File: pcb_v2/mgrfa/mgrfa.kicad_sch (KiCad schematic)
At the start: 20 parts, among them J1 sr8a_A, J10 designador, J2 sr8a_B, J3 sr8a_C, J4 sr8a_D, J5 sr8a_E, J6 sr8a_H, J7 sr8a_L, J8 bus_mgrf_1, J9 bus_mgrf_2, U1 74LS244, U2 74LS244

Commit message: arquivos no note
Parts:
- C1, C2: footprint (none) -> Capacitor_THT:C_Disc_D5.1mm_W3.2mm_P5.00mm

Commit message: projeto enviado para impressao em dezembro/25
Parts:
- D1: value LED -> POWER
- D2: value LED -> READ
- D3: value LED -> WRITE
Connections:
- net +5V: now also J8.1 (Pin_1); no longer J8.4 (Pin_4), J8.6 (Pin_6), J8.8 (Pin_8)
- net GND: now also J8.15 (Pin_15); no longer J8.10 (Pin_10), J8.12 (Pin_12), J8.14 (Pin_14)
- net data_0: now also J8.14 (Pin_14); no longer J8.15 (Pin_15)
- net data_7: now also J8.4 (Pin_4); no longer J8.1 (Pin_1)
- no-connect marks 46 -> 50

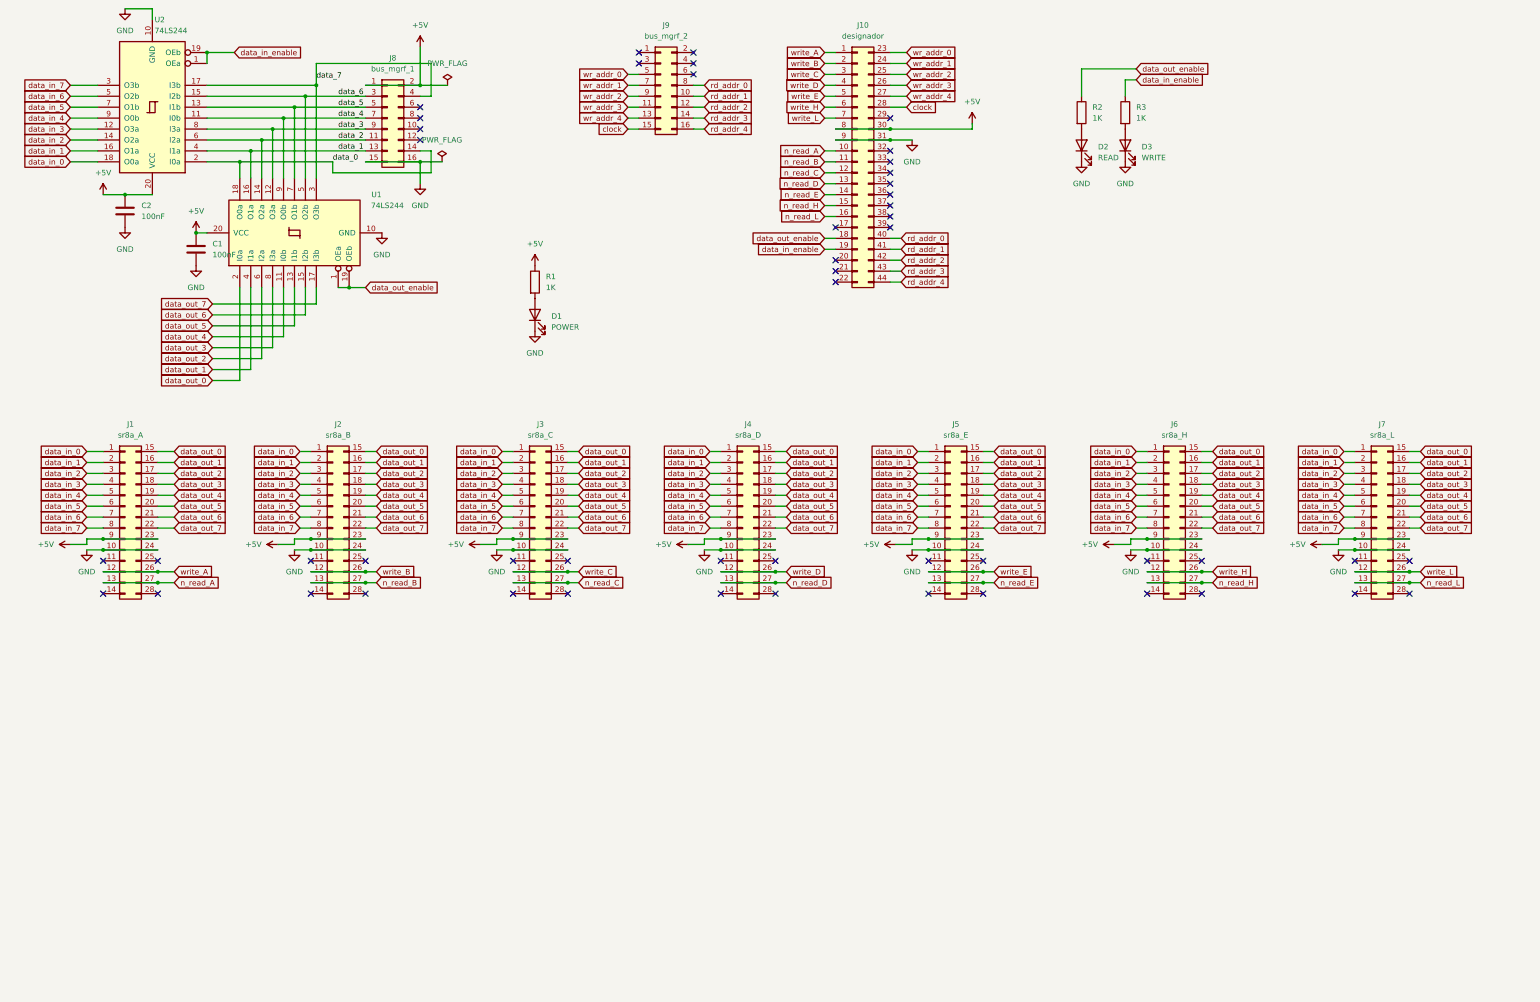
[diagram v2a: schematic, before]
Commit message: inicio da revisao completa; a placa sr8 será removida e incorporada aqui
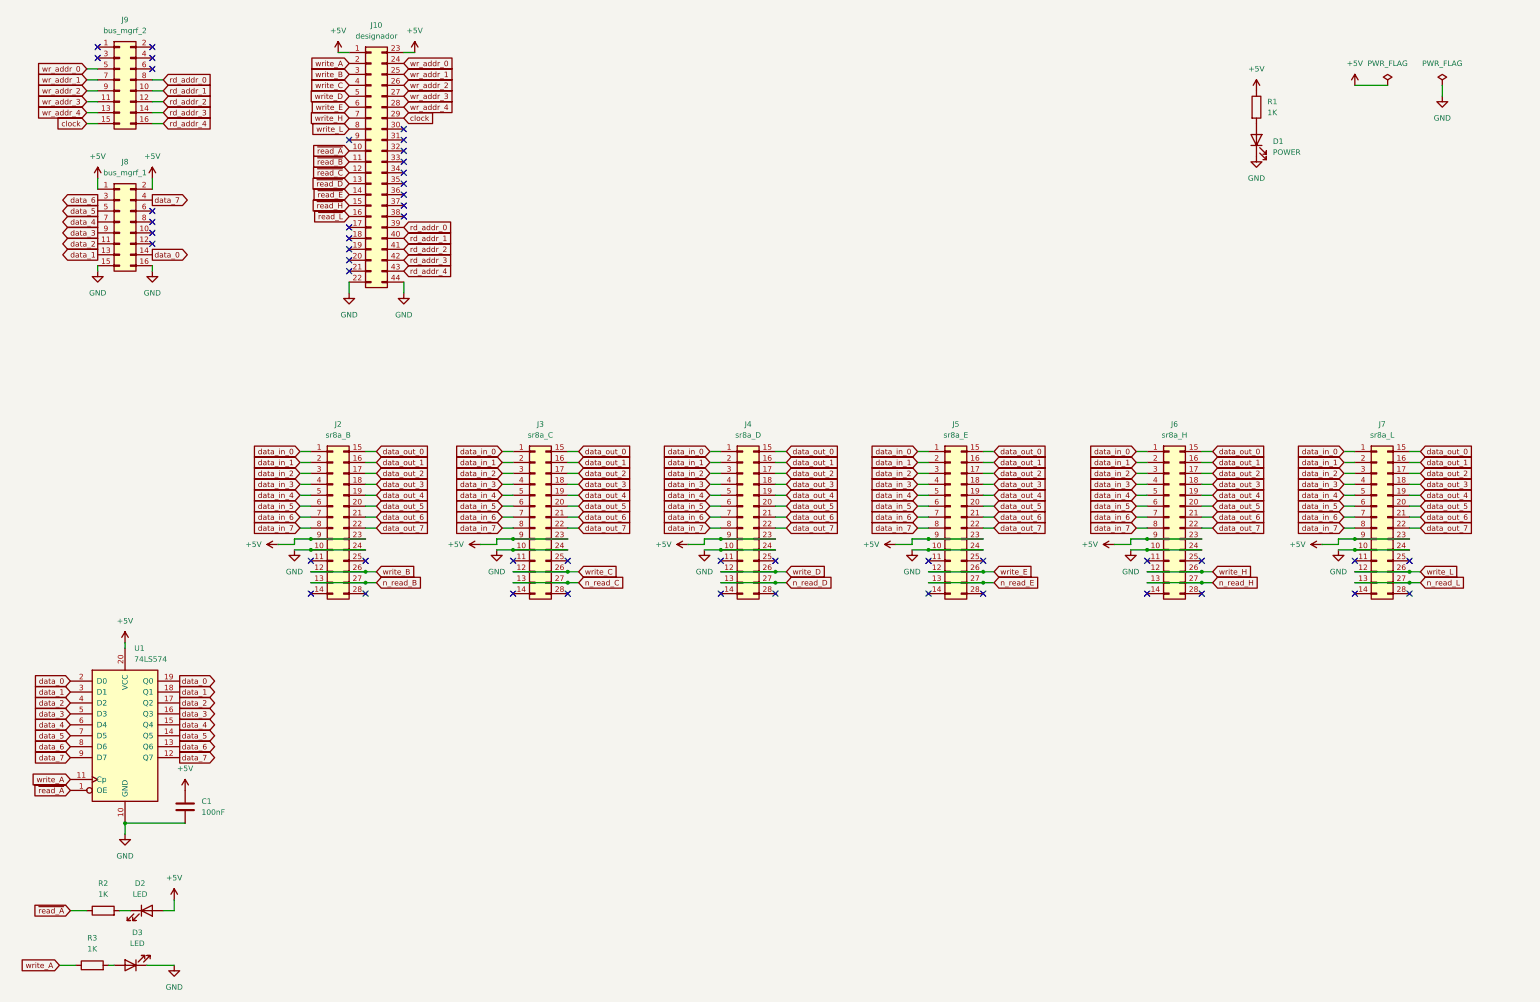
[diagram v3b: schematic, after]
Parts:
- removed C2: 100nF, Capacitor_THT:C_Disc_D5.1mm_W3.2mm_P5.00mm, symbol Device:C
- removed J1: sr8a_A, edge_connector:male-edge-connector-28, symbol Connector_Generic:Conn_02x14_Top_Bottom
- removed U1, U2: 74LS244, Package_DIP:DIP-20_W7.62mm, symbol 74xx:74LS244
- added U1: 74LS574, Package_DIP:DIP-20_W7.62mm, symbol 74xx:74LS574
- D2: value READ -> LED
- D3: value WRITE -> LED
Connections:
- net +5V: now also D2.2 (A), J10.1 (Pin_1), J10.23 (Pin_23), U1.20 (VCC); no longer J10.30 (Pin_30), J10.8 (Pin_8)
- net GND: now also J10.22 (Pin_22), J10.44 (Pin_44), U1.10 (GND); no longer D2.1 (K), J10.31 (Pin_31), J10.9 (Pin_9)
- net clock: now also J10.29 (Pin_29); no longer J10.28 (Pin_28)
- net data_0: now also U1.19 (Q0), U1.2 (D0)
- net data_1: now also U1.18 (Q1), U1.3 (D1)
- net data_2: now also U1.17 (Q2), U1.4 (D2)
- net data_3: now also U1.16 (Q3), U1.5 (D3)
- net data_4: now also U1.15 (Q4), U1.6 (D4)
- net data_5: now also U1.14 (Q5), U1.7 (D5)
- net data_6: now also U1.13 (Q6), U1.8 (D6)
- net data_7: now also U1.12 (Q7), U1.9 (D7)
- net n_read_B: no longer J10.11 (Pin_11)
- net n_read_C: no longer J10.12 (Pin_12)
- net n_read_D: no longer J10.13 (Pin_13)
- net n_read_E: no longer J10.14 (Pin_14)
- net n_read_H: no longer J10.15 (Pin_15)
- net n_read_L: no longer J10.16 (Pin_16)
- net rd_addr_0: now also J10.39 (Pin_39); no longer J10.40 (Pin_40)
- net rd_addr_1: now also J10.40 (Pin_40); no longer J10.41 (Pin_41)
- net rd_addr_2: now also J10.41 (Pin_41); no longer J10.42 (Pin_42)
- net rd_addr_3: now also J10.42 (Pin_42); no longer J10.43 (Pin_43)
- net rd_addr_4: now also J10.43 (Pin_43); no longer J10.44 (Pin_44)
- net wr_addr_0: now also J10.24 (Pin_24); no longer J10.23 (Pin_23)
- net wr_addr_1: now also J10.25 (Pin_25); no longer J10.24 (Pin_24)
- net wr_addr_2: now also J10.26 (Pin_26); no longer J10.25 (Pin_25)
- net wr_addr_3: now also J10.27 (Pin_27); no longer J10.26 (Pin_26)
- net wr_addr_4: now also J10.28 (Pin_28); no longer J10.27 (Pin_27)
- net write_A: now also J10.2 (Pin_2), R3.1, U1.11 (Cp); no longer J10.1 (Pin_1)
- net write_B: now also J10.3 (Pin_3); no longer J10.2 (Pin_2)
- net write_C: now also J10.4 (Pin_4); no longer J10.3 (Pin_3)
- net write_D: now also J10.5 (Pin_5); no longer J10.4 (Pin_4)
- net write_E: now also J10.6 (Pin_6); no longer J10.5 (Pin_5)
- net write_H: now also J10.7 (Pin_7); no longer J10.6 (Pin_6)
- net write_L: now also J10.8 (Pin_8); no longer J10.7 (Pin_7)
- net at R2.2: now also D2.1 (K); no longer D2.2 (A)
- net data_in_enable: no longer names the net of J10.19 (Pin_19)
- net data_in_enable: no longer R3.1
- net data_out_enable: no longer names the net of J10.18 (Pin_18)
- net data_out_enable: no longer R2.1
- net n_read_A renamed ~{read_A}
- net ~{read_A}: now also R2.1, U1.1 (OE)
- new net ~{read_B}: J10.11 (Pin_11)
- new net ~{read_C}: J10.12 (Pin_12)
- new net ~{read_D}: J10.13 (Pin_13)
- new net ~{read_E}: J10.14 (Pin_14)
- new net ~{read_H}: J10.15 (Pin_15)
- new net ~{read_L}: J10.16 (Pin_16)
- no-connect marks 50 -> 48
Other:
- moved on the sheet: D1, J10, J8, J9, R1

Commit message: revisao completa; mgrfa agora inclui sr8 e sgrda; remover estes dois no proximo commit
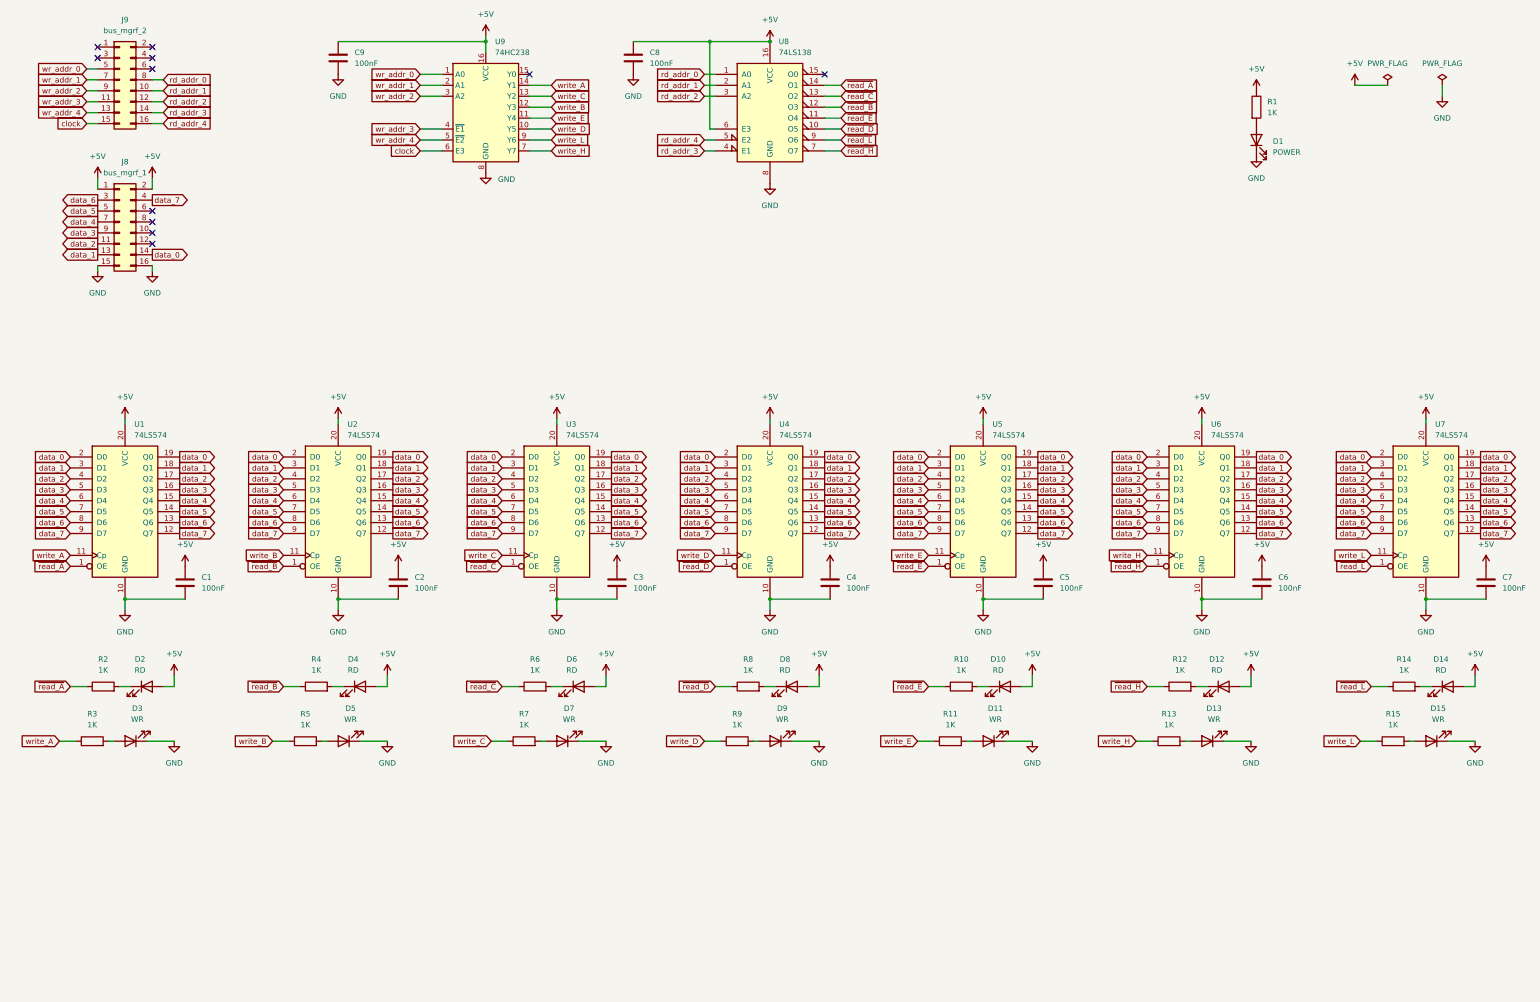
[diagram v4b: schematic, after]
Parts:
- removed J10: designador, edge_connector:male-edge-connector-44, symbol Connector_Generic:Conn_02x22_Top_Bottom
- removed J2: sr8a_B, edge_connector:male-edge-connector-28, symbol Connector_Generic:Conn_02x14_Top_Bottom
- removed J3: sr8a_C, edge_connector:male-edge-connector-28, symbol Connector_Generic:Conn_02x14_Top_Bottom
- removed J4: sr8a_D, edge_connector:male-edge-connector-28, symbol Connector_Generic:Conn_02x14_Top_Bottom
- removed J5: sr8a_E, edge_connector:male-edge-connector-28, symbol Connector_Generic:Conn_02x14_Top_Bottom
- removed J6: sr8a_H, edge_connector:male-edge-connector-28, symbol Connector_Generic:Conn_02x14_Top_Bottom
- removed J7: sr8a_L, edge_connector:male-edge-connector-28, symbol Connector_Generic:Conn_02x14_Top_Bottom
- added C2, C3, C4, C5, C6, C7: 100nF, Capacitor_THT:C_Disc_D5.1mm_W3.2mm_P5.00mm, symbol Device:C
- added C8, C9: 100nF, Capacitor_THT:C_Disc_D4.7mm_W2.5mm_P5.00mm, symbol Device:C
- added D10, D12, D14, D4, D6, D8: RD, LED_THT:LED_D5.0mm, symbol Device:LED
- added D11, D13, D15, D5, D7, D9: WR, LED_THT:LED_D5.0mm, symbol Device:LED
- added R10, R11, R12, R13, R14, R15, R4, R5, R6, R7, R8, R9: 1K, Resistor_THT:R_Axial_DIN0207_L6.3mm_D2.5mm_P7.62mm_Horizontal, symbol Device:R
- added U2, U3, U4, U5, U6, U7: 74LS574, Package_DIP:DIP-20_W7.62mm, symbol 74xx:74LS574
- added U8: 74LS138, Package_DIP:DIP-16_W7.62mm, symbol 74xx:74LS138
- added U9: 74HC238, Package_DIP:DIP-16_W7.62mm, symbol 74xx:74HC238
- D2: value LED -> RD
- D3: value LED -> WR
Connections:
- net +5V: now also C2.1, C3.1, C4.1, C5.1, C6.1, C7.1, C8.1, C9.1, D10.2 (A), D12.2 (A), D14.2 (A), D4.2 (A), D6.2 (A), D8.2 (A), U2.20 (VCC), U3.20 (VCC), U4.20 (VCC), U5.20 (VCC), U6.20 (VCC), U7.20 (VCC), U8.16 (VCC), U8.6 (E3), U9.16 (VCC)
- net GND: now also C2.2, C3.2, C4.2, C5.2, C6.2, C7.2, C8.2, C9.2, D11.1 (K), D13.1 (K), D15.1 (K), D5.1 (K), D7.1 (K), D9.1 (K), U2.10 (GND), U3.10 (GND), U4.10 (GND), U5.10 (GND), U6.10 (GND), U7.10 (GND), U8.8 (GND), U9.8 (GND)
- net clock: now also U9.6 (E3)
- net data_0: now also U2.19 (Q0), U2.2 (D0), U3.19 (Q0), U3.2 (D0), U4.19 (Q0), U4.2 (D0), U5.19 (Q0), U5.2 (D0), U6.19 (Q0), U6.2 (D0), U7.19 (Q0), U7.2 (D0)
- net data_1: now also U2.18 (Q1), U2.3 (D1), U3.18 (Q1), U3.3 (D1), U4.18 (Q1), U4.3 (D1), U5.18 (Q1), U5.3 (D1), U6.18 (Q1), U6.3 (D1), U7.18 (Q1), U7.3 (D1)
- net data_2: now also U2.17 (Q2), U2.4 (D2), U3.17 (Q2), U3.4 (D2), U4.17 (Q2), U4.4 (D2), U5.17 (Q2), U5.4 (D2), U6.17 (Q2), U6.4 (D2), U7.17 (Q2), U7.4 (D2)
- net data_3: now also U2.16 (Q3), U2.5 (D3), U3.16 (Q3), U3.5 (D3), U4.16 (Q3), U4.5 (D3), U5.16 (Q3), U5.5 (D3), U6.16 (Q3), U6.5 (D3), U7.16 (Q3), U7.5 (D3)
- net data_4: now also U2.15 (Q4), U2.6 (D4), U3.15 (Q4), U3.6 (D4), U4.15 (Q4), U4.6 (D4), U5.15 (Q4), U5.6 (D4), U6.15 (Q4), U6.6 (D4), U7.15 (Q4), U7.6 (D4)
- net data_5: now also U2.14 (Q5), U2.7 (D5), U3.14 (Q5), U3.7 (D5), U4.14 (Q5), U4.7 (D5), U5.14 (Q5), U5.7 (D5), U6.14 (Q5), U6.7 (D5), U7.14 (Q5), U7.7 (D5)
- net data_6: now also U2.13 (Q6), U2.8 (D6), U3.13 (Q6), U3.8 (D6), U4.13 (Q6), U4.8 (D6), U5.13 (Q6), U5.8 (D6), U6.13 (Q6), U6.8 (D6), U7.13 (Q6), U7.8 (D6)
- net data_7: now also U2.12 (Q7), U2.9 (D7), U3.12 (Q7), U3.9 (D7), U4.12 (Q7), U4.9 (D7), U5.12 (Q7), U5.9 (D7), U6.12 (Q7), U6.9 (D7), U7.12 (Q7), U7.9 (D7)
- net rd_addr_0: now also U8.1 (A0)
- net rd_addr_1: now also U8.2 (A1)
- net rd_addr_2: now also U8.3 (A2)
- net rd_addr_3: now also U8.4 (E1)
- net rd_addr_4: now also U8.5 (E2)
- net wr_addr_0: now also U9.1 (A0)
- net wr_addr_1: now also U9.2 (A1)
- net wr_addr_2: now also U9.3 (A2)
- net wr_addr_3: now also U9.4 (~{E1})
- net wr_addr_4: now also U9.5 (~{E2})
- net write_A: now also U9.14 (Y1)
- net write_B: now also R5.1, U2.11 (Cp), U9.12 (Y3)
- net write_C: now also R7.1, U3.11 (Cp), U9.13 (Y2)
- net write_D: now also R9.1, U4.11 (Cp), U9.10 (Y5)
- net write_E: now also R11.1, U5.11 (Cp), U9.11 (Y4)
- net write_H: now also R13.1, U6.11 (Cp), U9.7 (Y7)
- net write_L: now also R15.1, U7.11 (Cp), U9.9 (Y6)
- net ~{read_A}: now also U8.14 (O1)
- net ~{read_B}: now also R4.1, U2.1 (OE), U8.12 (O3)
- net ~{read_C}: now also R6.1, U3.1 (OE), U8.13 (O2)
- net ~{read_D}: now also R8.1, U4.1 (OE), U8.10 (O5)
- net ~{read_E}: now also R10.1, U5.1 (OE), U8.11 (O4)
- net ~{read_H}: now also R12.1, U6.1 (OE), U8.7 (O7)
- net ~{read_L}: now also R14.1, U7.1 (OE), U8.9 (O6)
- new net: D5.2 (A), R5.2
- new net: D6.1 (K), R6.2
- new net: D4.1 (K), R4.2
- new net: D7.2 (A), R7.2
- new net: D8.1 (K), R8.2
- new net: D14.1 (K), R14.2
- new net: D11.2 (A), R11.2
- new net: D12.1 (K), R12.2
- new net: D15.2 (A), R15.2
- new net: D9.2 (A), R9.2
- new net: D10.1 (K), R10.2
- new net: D13.2 (A), R13.2
- no-connect marks 48 -> 11
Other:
- moved on the sheet: C1, D2, D3, R2, R3, U1
